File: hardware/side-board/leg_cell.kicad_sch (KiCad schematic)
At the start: 85 parts, among them IC201 STM32C092KCT6, IC202 TCAN332DR, IC203 TPS56A37RPAR, IC204 INA181A1IDBVR, J201 Servo Connector, J202 Servo Connector, J203 Servo Connector, J204 TC2050, J205 Conn_01x06, Y201 Crystal_GND24

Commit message: side board: 1206 cell fuse, test points
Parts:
- F201: footprint (none) -> Fuse:Fuse_1206_3216Metric
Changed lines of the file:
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@@
 			)
 		)
-		(property "Footprint" ""
+		(property "Footprint" "Fuse:Fuse_1206_3216Metric"
 			(at 264.16 68.58 0)
 			(hide yes)

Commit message: side board: amrm inductors, 1206 buck input cap, xh can connector, rt no-connect
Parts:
- C214: value 15u -> 15u 35V; footprint Capacitor_SMD:C_0805_2012Metric -> Capacitor_SMD:C_1206_3216Metric
- C218, C219: footprint Capacitor_SMD:C_0805_2012Metric -> Capacitor_SMD:C_1206_3216Metric
- C220, C221: value 10p -> 18p
- L201: footprint (none) -> vector:INDPM116102X400N; Manufacturer_Part_Number (none) -> AMRM001010404R7MA1
- R227, R228: value 10k -> 2.2k
- Y201: Manufacturer_Part_Number (none) -> K2B400001210

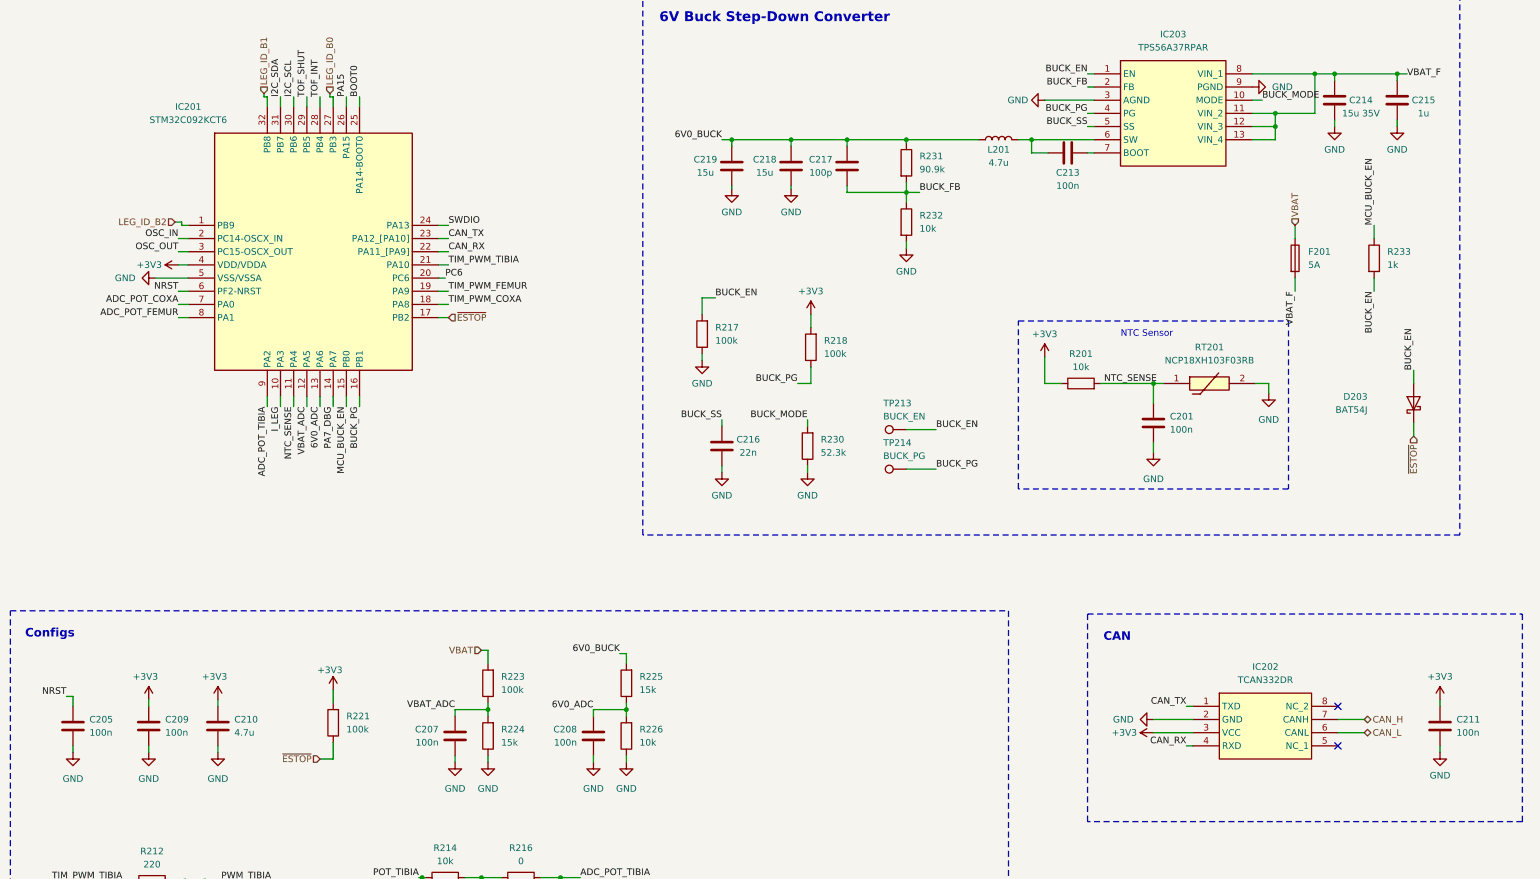
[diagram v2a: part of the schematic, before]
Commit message: Updated PCB of side-board
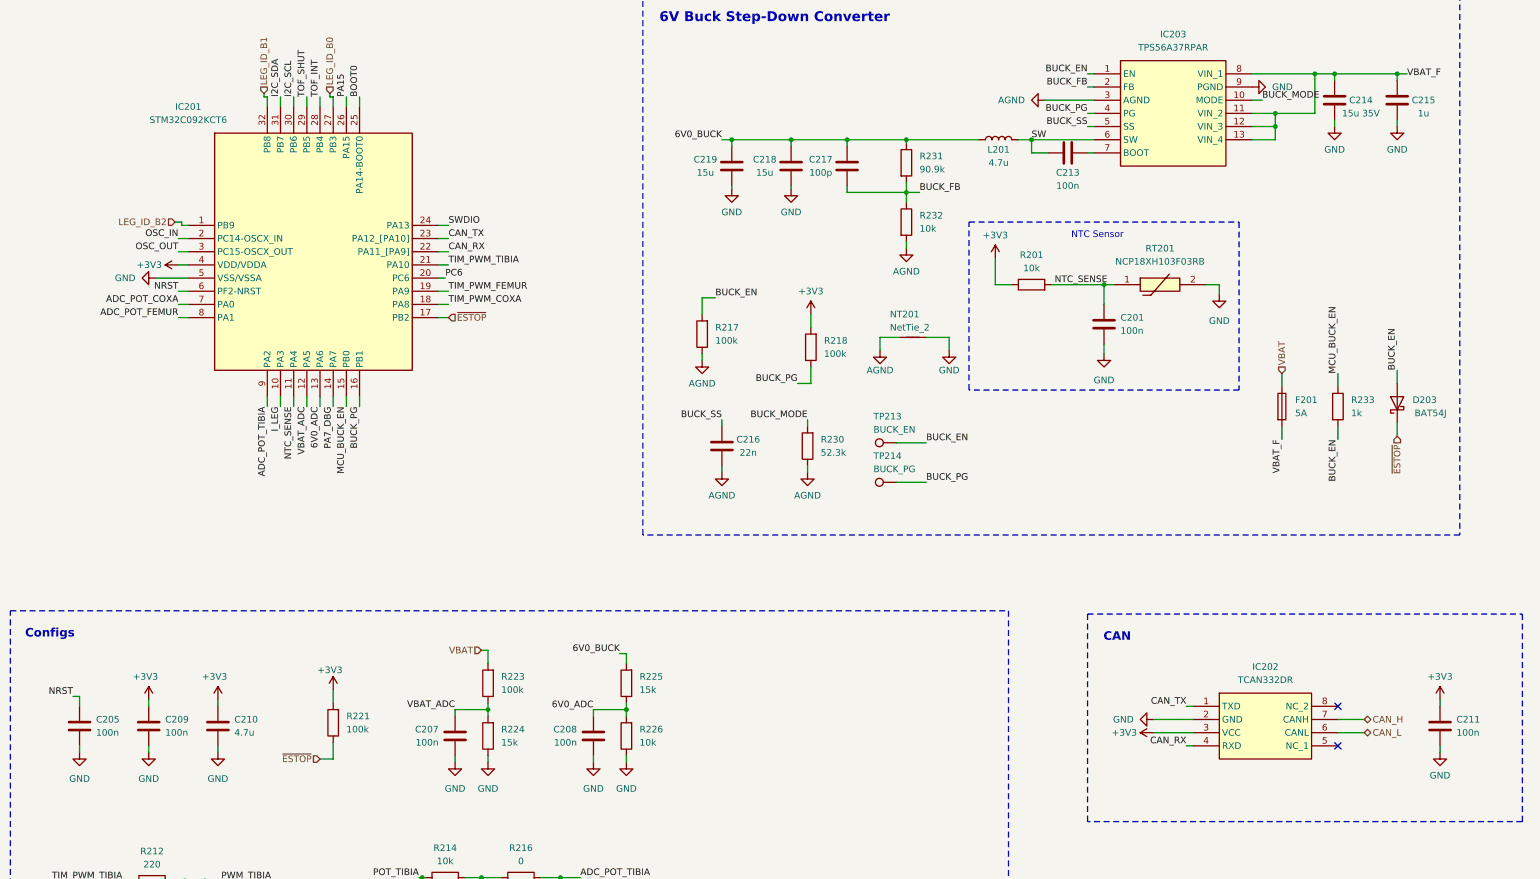
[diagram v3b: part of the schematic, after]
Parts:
- added NT201: NetTie_2, NetTie:NetTie-2_SMD_Pad0.5mm, symbol Device:NetTie_2
- C205, C206, C207, C208, C209, C211, C212, C213, C216, C220, C221: footprint Capacitor_SMD:C_0805_2012Metric -> Capacitor_SMD:C_0603_1608Metric
- C217: footprint Capacitor_SMD:C_0805_2012Metric -> Resistor_SMD:R_0603_1608Metric
- J201, J202, J203: footprint Connector_JST:JST_XH_S4B-XH-A-1_1x04_P2.50mm_Horizontal -> Connector_JST:JST_XH_B4B-XH-A_1x04_P2.50mm_Vertical
- R231, R232: footprint Resistor_SMD:R_0805_2012Metric -> Resistor_SMD:R_0603_1608Metric
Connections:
- net GND: now also NT201.2; no longer C216.2, IC203.3 (AGND), R217.1, R230.1, R232.2
- net SW: now reaches C213.2, IC203.6 (SW), L201.2
- new net AGND: C216.2, IC203.3 (AGND), NT201.1, R217.1, R230.1, R232.2
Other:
- moved on the sheet: C201, C205, D203, F201, R201, R233, RT201, TP213, TP214

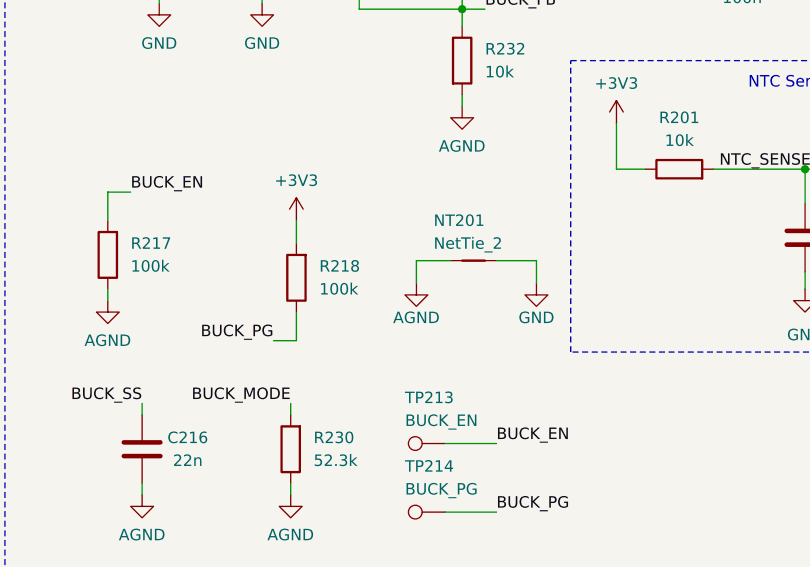
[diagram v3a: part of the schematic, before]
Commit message: Updated PCB placement side-board
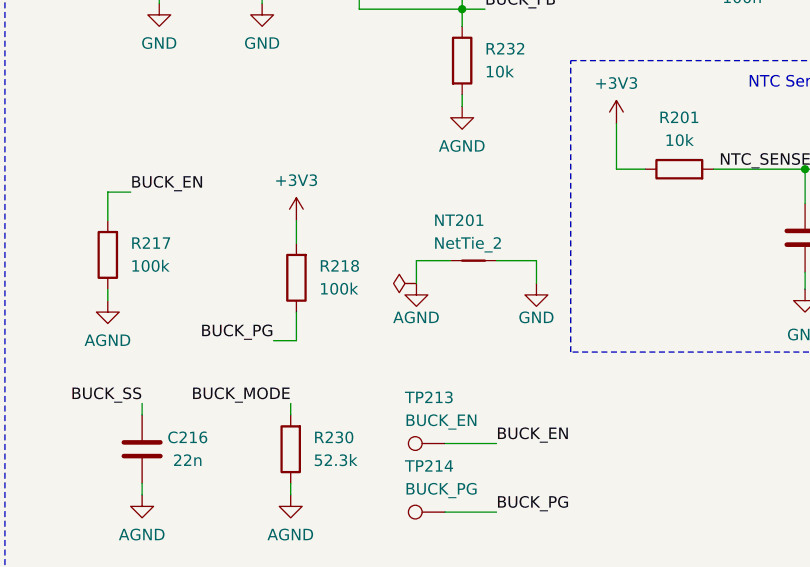
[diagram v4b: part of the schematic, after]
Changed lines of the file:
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@@
 	)
 	(symbol
-		(lib_id "power:GND")
+		(lib_id "vector-power:AGND")
 		(at 149.86 88.265 0)
 		(unit 1)
@@
 	)
 	(symbol
-		(lib_id "power:GND")
+		(lib_id "vector-power:AGND")
 		(at 153.67 109.855 0)
 		(unit 1)
@@
 	)
 	(symbol
-		(lib_id "power:GND")
+		(lib_id "vector-power:AGND")
 		(at 184.15 86.36 0)
 		(unit 1)
@@
 	)
 	(symbol
-		(lib_id "power:GND")
+		(lib_id "vector-power:AGND")
 		(at 215.9 38.1 270)
 		(unit 1)
@@
 	)
 	(symbol
-		(lib_id "power:GND")
+		(lib_id "vector-power:AGND")
 		(at 170.18 109.855 0)
 		(unit 1)
@@
 	)
 	(symbol
-		(lib_id "power:GND")
+		(lib_id "vector-power:AGND")
 		(at 189.23 66.675 0)
 		(unit 1)
@@
 					(unit 1)
 				)
+			)
+		)
+	)
+	(symbol
+		(lib_id "power:PWR_FLAG")
+		(at 184.15 86.36 90)
+		(unit 1)
+		(body_style 1)
+		(exclude_from_sim no)
+		(in_bom yes)
+		(on_board yes)
+		(in_pos_files yes)
+		(dnp no)
+		(property "Reference" "#FLG0201"
+			(at 182.245 86.36 0)
+			(hide yes)
+			(show_name no)
+			(do_not_autoplace no)
+			(effects
+				(font
+					(size 1.27 1.27)
+				)
+			)
+		)
+		(property "Value" "PWR_FLAG"
+			(at 173.99 86.995 0)
+			(hide yes)
+			(show_name no)
+			(do_not_autoplace no)
+			(effects
+				(font
+					(size 1.27 1.27)
+				)
+			)
+		)
+		(pin "1"
+		)
+		(instances
+			(project "side-board"
+				(path "/f4a3e594-e59c-4d07-8b29-d9b2c0e13b64/ed134523-9e05-457c-ab50-dc2cbf503568"
+					(reference "#FLG0201")
+					(unit 1)
+				)
+				(path "/f4a3e594-e59c-4d07-8b29-d9b2c0e13b64/e9e2a06a-b123-4760-909f-4357b6b61804"
+					(reference "#FLG0301")
+					(unit 1)
+				)
+				(path "/f4a3e594-e59c-4d07-8b29-d9b2c0e13b64/1f5fead0-6287-4b95-a2a4-ee2ca8c4688f"
+					(reference "#FLG0401")
+					(unit 1)
+				)

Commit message: Updated sideboard PCB
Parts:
- L201: footprint vector:INDPM116102X400N -> side-board:INDPM7973X540N; Manufacturer_Part_Number AMRM001010404R7MA1 -> SRP7050WA-4R7M
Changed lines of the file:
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@@
 	)
 	(symbol
+		(lib_id "power:PWR_FLAG")
+		(at 184.15 86.36 90)
+		(unit 1)
+		(body_style 1)
+		(exclude_from_sim no)
+		(in_bom yes)
+		(on_board yes)
+		(in_pos_files yes)
+		(dnp no)
+		(property "Reference" "#FLG0201"
+			(at 182.245 86.36 0)
+			(hide yes)
+			(show_name no)
+			(do_not_autoplace no)
+			(effects
+				(font
+					(size 1.27 1.27)
+				)
+			)
+		)
+		(property "Value" "PWR_FLAG"
+			(at 173.99 86.995 0)
+			(hide yes)
+			(show_name no)
+			(do_not_autoplace no)
+			(effects
+				(font
+					(size 1.27 1.27)
+				)
+			)
+		)
+		(property "Footprint" ""
+			(at 184.15 86.36 0)
+			(show_name no)
+			(do_not_autoplace no)
+			(effects
+				(font
+					(size 1.27 1.27)
+				)
+			)
+		)
+		(property "Datasheet" ""
+			(at 184.15 86.36 0)
+			(show_name no)
+			(do_not_autoplace no)
+			(effects
+				(font
+					(size 1.27 1.27)
+				)
+			)
+		)
+		(property "Description" ""
+			(at 184.15 86.36 0)
+			(show_name no)
+			(do_not_autoplace no)
+			(effects
+				(font
+					(size 1.27 1.27)
+				)
+			)
+		)
+		(pin "1"
+		)
+		(instances
+			(project "side-board"
+				(path "/f4a3e594-e59c-4d07-8b29-d9b2c0e13b64/1f5fead0-6287-4b95-a2a4-ee2ca8c4688f"
+					(reference "#FLG0401")
+					(unit 1)
+				)
+				(path "/f4a3e594-e59c-4d07-8b29-d9b2c0e13b64/e9e2a06a-b123-4760-909f-4357b6b61804"
+					(reference "#FLG0301")
+					(unit 1)
+				)
+				(path "/f4a3e594-e59c-4d07-8b29-d9b2c0e13b64/ed134523-9e05-457c-ab50-dc2cbf503568"
+					(reference "#FLG0201")
+					(unit 1)
+				)
+			)
+		)
+	)
+	(symbol
 		(lib_id "power:GND")
 		(at 283.845 43.18 0)
@@
 			)
 		)
-		(property "Footprint" "vector:INDPM116102X400N"
+		(property "Footprint" "side-board:INDPM7973X540N"
 			(at 207.01 45.72 0)
 			(hide yes)
@@
 			)
 		)
-		(property "Manufacturer_Part_Number" "AMRM001010404R7MA1"
+		(property "Manufacturer_Part_Number" "SRP7050WA-4R7M"
 			(at 207.01 45.72 0)
 			(hide yes)
@@
 					(unit 1)
 				)
-			)
-		)
-	)
-	(symbol
-		(lib_id "power:PWR_FLAG")
-		(at 184.15 86.36 90)
-		(unit 1)
-		(body_style 1)
-		(exclude_from_sim no)
-		(in_bom yes)
-		(on_board yes)
-		(in_pos_files yes)
-		(dnp no)
-		(property "Reference" "#FLG0201"
-			(at 182.245 86.36 0)
-			(hide yes)
-			(show_name no)
-			(do_not_autoplace no)
-			(effects
-				(font
-					(size 1.27 1.27)
-				)
-			)
-		)
-		(property "Value" "PWR_FLAG"
-			(at 173.99 86.995 0)
-			(hide yes)
-			(show_name no)
-			(do_not_autoplace no)
-			(effects
-				(font
-					(size 1.27 1.27)
-				)
-			)
-		)
-		(pin "1"
-		)
-		(instances
-			(project "side-board"
-				(path "/f4a3e594-e59c-4d07-8b29-d9b2c0e13b64/ed134523-9e05-457c-ab50-dc2cbf503568"
-					(reference "#FLG0201")
-					(unit 1)
-				)
-				(path "/f4a3e594-e59c-4d07-8b29-d9b2c0e13b64/e9e2a06a-b123-4760-909f-4357b6b61804"
-					(reference "#FLG0301")
-					(unit 1)
-				)
-				(path "/f4a3e594-e59c-4d07-8b29-d9b2c0e13b64/1f5fead0-6287-4b95-a2a4-ee2ca8c4688f"
-					(reference "#FLG0401")
-					(unit 1)
-				)

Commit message: Updated PCB placement sideboard
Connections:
- net ADC_POT_COXA: now also R204.1; no longer R204.2
- net at R202.2, R203.2: now also R204.2; no longer R204.1
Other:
- moved on the sheet: R204
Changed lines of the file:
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@@
 	(symbol
 		(lib_id "Device:R")
-		(at 114.935 255.905 90)
+		(at 114.935 255.905 270)
+		(mirror x)
 		(unit 1)
 		(body_style 1)
@@
 		(in_pos_files yes)
 		(dnp no)
-		(fields_autoplaced yes)
 		(property "Reference" "R204"
 			(at 114.935 250.19 90)

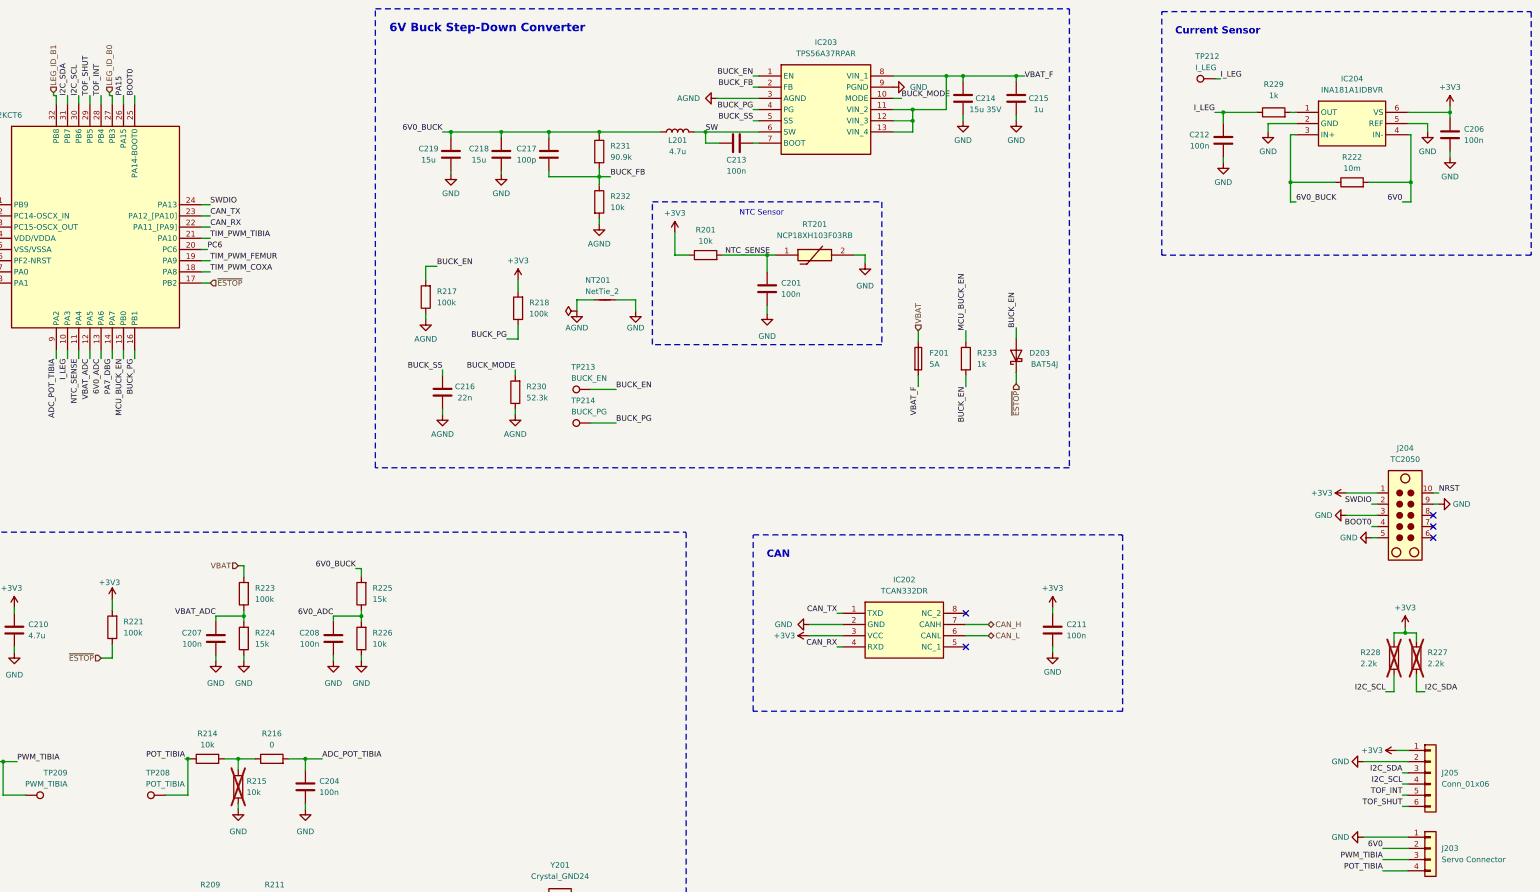
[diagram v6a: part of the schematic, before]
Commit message: Compacted side board pcb
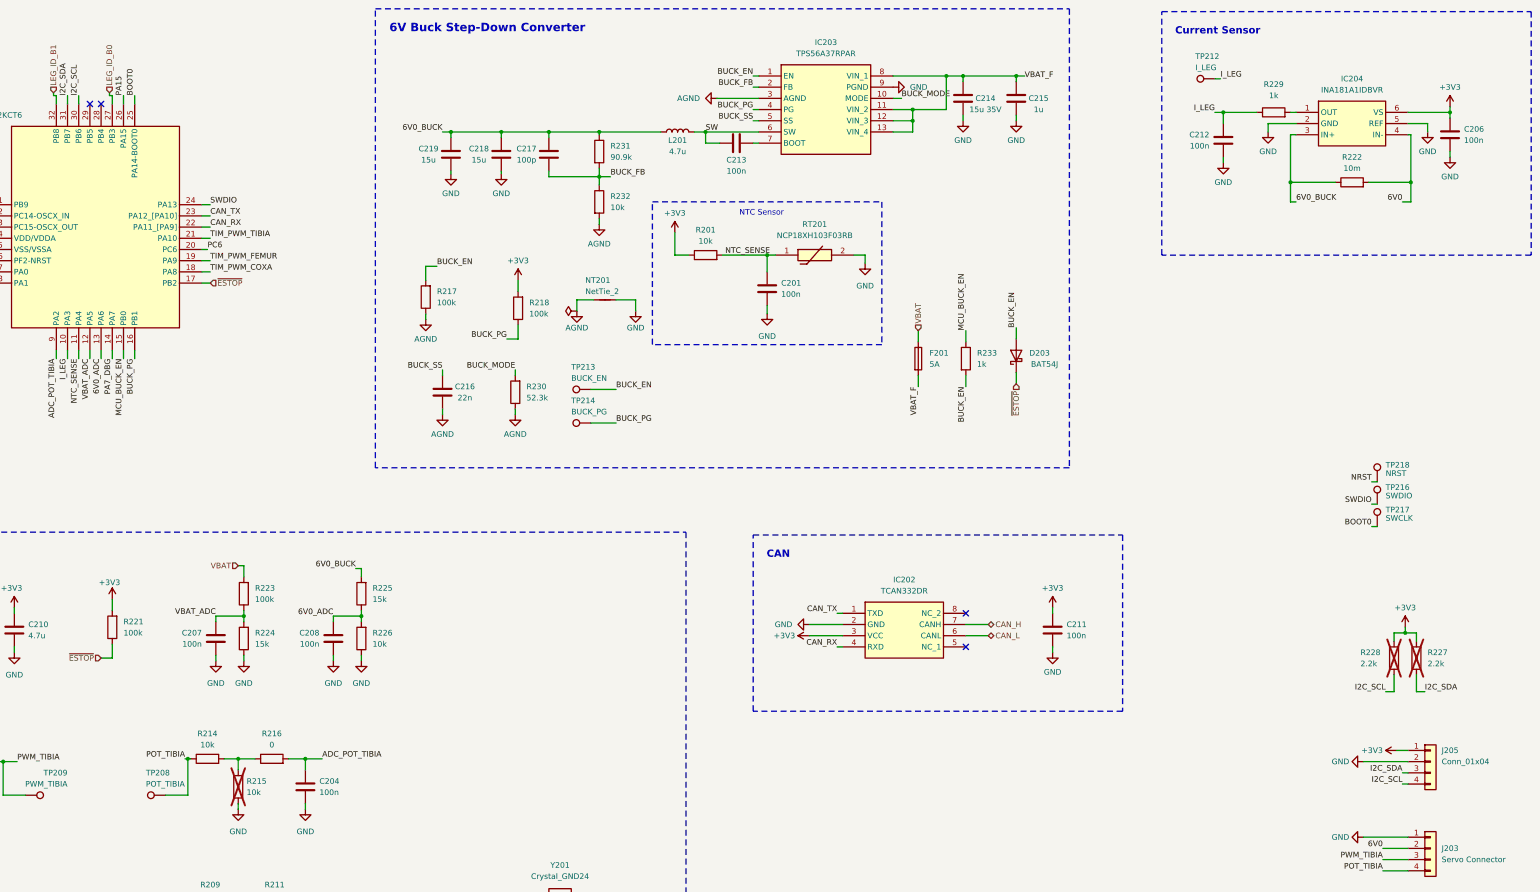
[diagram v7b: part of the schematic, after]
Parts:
- removed J204: TC2050, Connector:Tag-Connect_TC2050-IDC-FP_2x05_P1.27mm_Vertical, symbol Connector:TC2050
- added TP216: SWDIO, TestPoint:TestPoint_Pad_D1.0mm, symbol Connector:TestPoint
- added TP217: SWCLK, TestPoint:TestPoint_Pad_D1.0mm, symbol Connector:TestPoint
- added TP218: NRST, TestPoint:TestPoint_Pad_D1.0mm, symbol Connector:TestPoint
- C201, C202, C203, C204, C205, C206, C207, C208, C209, C211, C212, C213, C216, C220, C221: footprint Capacitor_SMD:C_0603_1608Metric -> Capacitor_SMD:C_0402_1005Metric
- C217: footprint Resistor_SMD:R_0603_1608Metric -> Capacitor_SMD:C_0402_1005Metric
- J205: value Conn_01x06 -> Conn_01x04; footprint Connector_JST:JST_XH_B6B-XH-A_1x06_P2.50mm_Vertical -> Connector_JST:JST_XH_B4B-XH-A_1x04_P2.50mm_Vertical; symbol Connector_Generic:Conn_01x06 -> Connector_Generic:Conn_01x04
- R201, R202, R203, R204, R205, R206, R207, R208, R209, R210, R211, R212, R213, R214, R215, R216, R217, R218, R219, R220, R221, R223, R224, R225, R226, R227, R228, R229, R230, R231, R232, R233: footprint Resistor_SMD:R_0603_1608Metric -> Resistor_SMD:R_0402_1005Metric
- TP201, TP202, TP203, TP204, TP205, TP206, TP207, TP208, TP209, TP210, TP211, TP212, TP213, TP214, TP215: footprint TestPoint:TestPoint_Pad_D2.0mm -> TestPoint:TestPoint_Pad_D1.0mm
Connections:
- net BOOT0: now also TP217.1
- net NRST: now also TP218.1
- net SWDIO: now also TP216.1
- net TOF_INT: no longer names the net of IC201.28 (PB4)
- net TOF_INT: no longer J205.5 (Pin_5)
- net TOF_SHUT: no longer names the net of IC201.29 (PB5)
- net TOF_SHUT: no longer J205.6 (Pin_6)
- no-connect marks 5 -> 4
